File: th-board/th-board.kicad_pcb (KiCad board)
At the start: 2 copper layers, 59.5 x 48.5 mm, 21 parts, among them J1 Conn_01x02, J2 Conn_01x04, U1 ESP-12F, U2 DHT11, U3 SPX3819M5-L

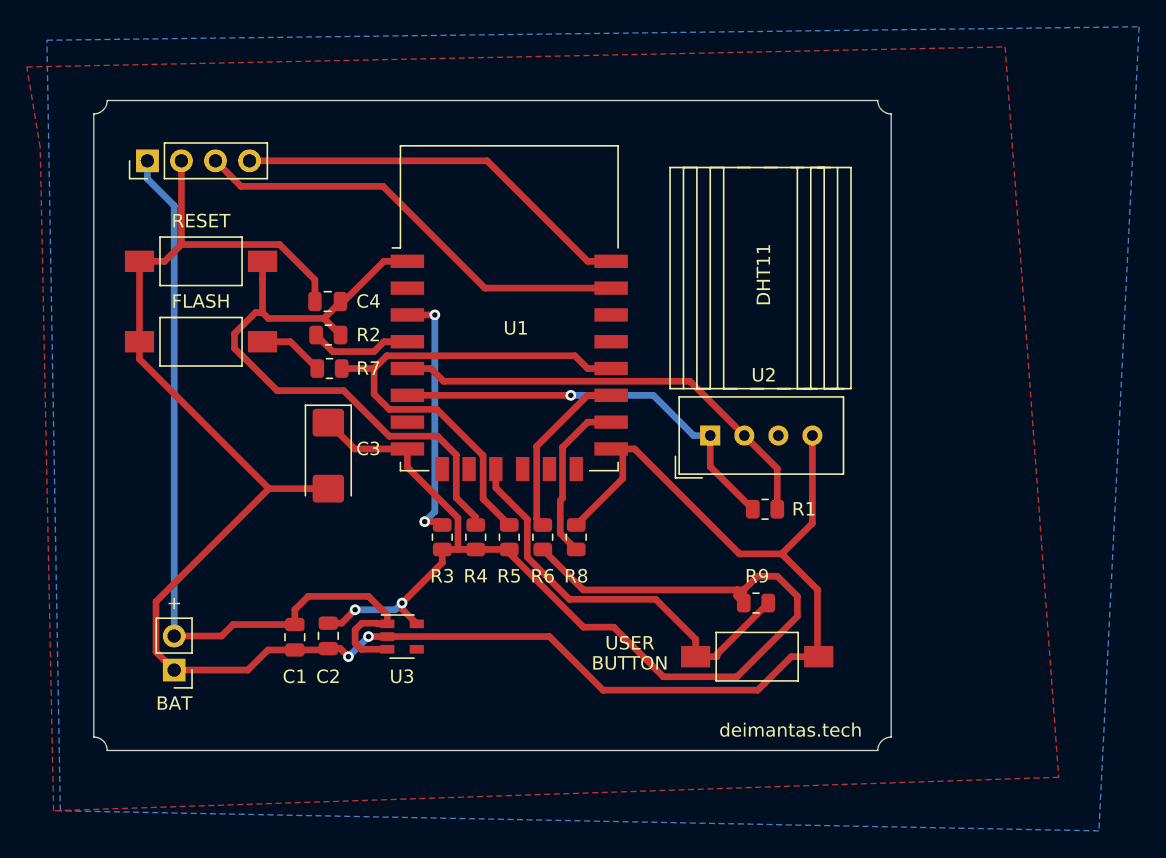
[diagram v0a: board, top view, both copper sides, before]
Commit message: Led added to pcb, v1.1
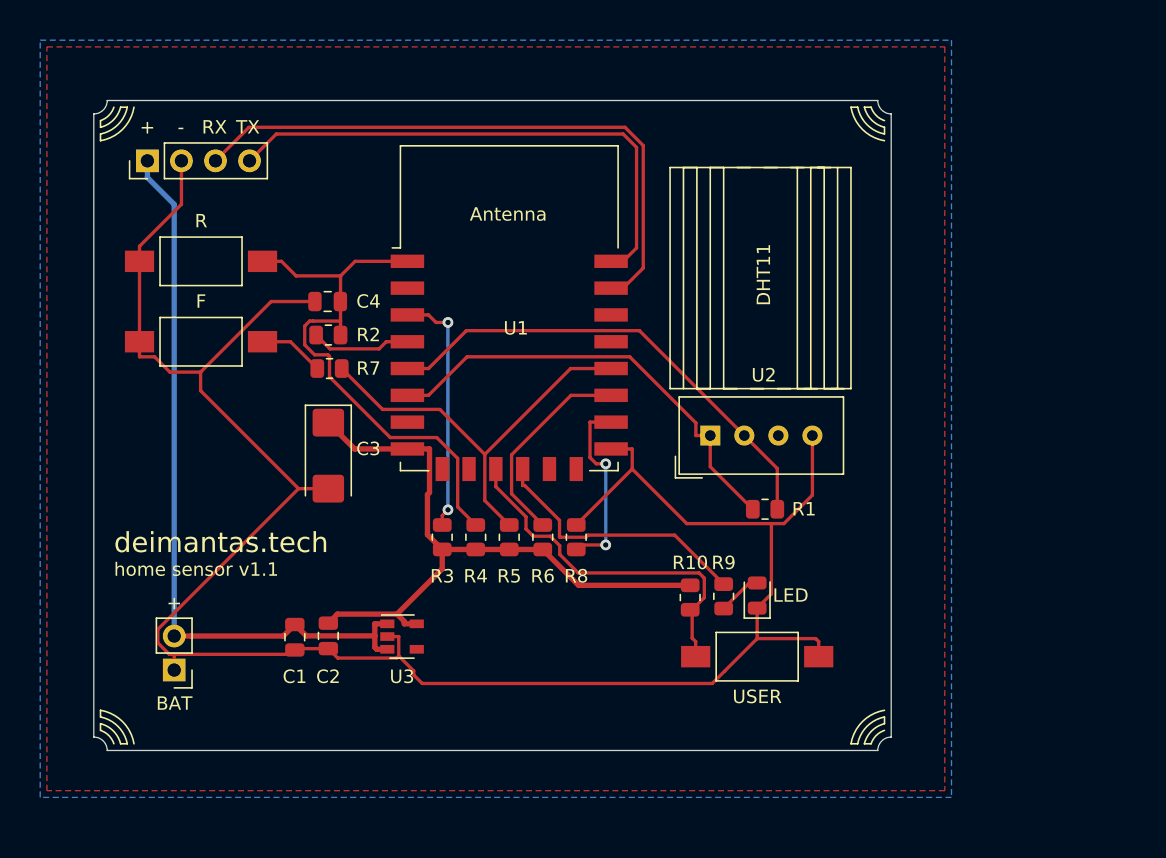
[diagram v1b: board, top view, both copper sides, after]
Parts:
- added D1: LED, LED_SMD:LED_0805_2012Metric, F.Cu at (168.5, 111.9)
- added R10: R470, Resistor_SMD:R_0805_2012Metric, F.Cu at (166.0, 112.0)
- moved R9 4.93 mm to (163.5, 112.1), turned to 90 degrees
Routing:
- net VCC: track 87.3 -> 49.5 mm, vias 2 -> 0
- net Net-(R10-Pad2): track 0.00 -> 20.1 mm
- net RX: track 33.5 -> 45.7 mm
- net TX: track 30.1 -> 39.9 mm
- net Net-(R5-Pad2): track 38.8 -> 31.4 mm
- net RST: track 48.0 -> 41.7 mm
- net Net-(C1-Pad1): track 61.5 -> 55.6 mm
- net Net-(R9-Pad1): track 31.1 -> 27.1 mm
- net Net-(D1-Pad2): track 0.00 -> 3.29 mm
- net DHT11_VCC: track 30.7 -> 33.6 mm, vias 1 -> 0
- net DHT11_IO: track 33.7 -> 36.1 mm
- net Net-(R6-Pad2): track 13.2 -> 15.5 mm
- net GND: track 159.5 -> 157.2 mm, vias 2 -> 0
- net Net-(R8-Pad1): track 12.6 -> 14.0 mm, vias 0 -> 2
- net Net-(R3-Pad2): track 19.2 -> 18.6 mm
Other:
- net class Default: trace_width 0.5 -> 0.25
- net class vcc added: clearance 0.2, trace_width 0.4, via_dia 0.8, via_drill 0.4
- board text added: "-"
- board text added: "F"
- board text added: "R"
- board text added: "RX"
- board text added: "TX"
- board text added: "home sensor v1.1"
- board text removed: "BUTTON"
- board text removed: "FLASH"
- board text removed: "RESET"

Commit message: PCB: new board
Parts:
- moved U2 76.5 mm to (241.5, 97.5)
- moved U1 75.8 mm to (225.8, 88.2)
- moved C1 75.0 mm to (209.0, 112.8)
- moved C2 75.0 mm to (211.5, 112.7)
- moved C3 75.0 mm to (211.5, 99.2)
- moved C4 75.0 mm to (211.4, 87.8)
- moved D1 75.0 mm to (243.5, 109.7)
- moved R1 75.0 mm to (244.1, 103.2)
- moved R10 75.0 mm to (241.0, 109.8)
- moved R2 75.0 mm to (211.5, 90.2)
- moved R3 75.0 mm to (220.0, 105.3)
- moved R4 75.0 mm to (222.5, 105.3)
- moved R5 75.0 mm to (225.0, 105.3)
- moved R6 75.0 mm to (227.5, 105.3)
- moved R7 75.0 mm to (211.6, 92.8)
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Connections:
- R10 pad 2: Net-(R10-Pad2) -> USER_LED
- R9 pad 1: Net-(R9-Pad1) -> USER_BUTTON
- SW_User2 pad 2: Net-(R9-Pad1) -> USER_BUTTON
- U1 pad 11: Net-(R9-Pad1) -> Net-(U1-Pad11)
- U1 pad 12: Net-(R10-Pad2) -> Net-(U1-Pad12)
- U1 pad 19: Net-(U1-Pad19) -> USER_BUTTON
- U1 pad 20: Net-(U1-Pad20) -> USER_LED
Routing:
- net GND: track 157.2 -> 194.4 mm, vias 0 -> 1
- net USER_BUTTON: track 0.00 -> 36.0 mm
- net USER_LED: track 0.00 -> 32.8 mm
- net Net-(R9-Pad1): track 27.1 -> 0.00 mm
- net Net-(R10-Pad2): track 20.1 -> 0.00 mm
- net Net-(C1-Pad1): track 55.6 -> 73.7 mm
- net RX: track 45.7 -> 35.8 mm
- net VCC: track 49.5 -> 57.5 mm
- net TX: track 39.9 -> 32.1 mm
- net Net-(R3-Pad2): track 18.6 -> 24.7 mm
- net Net-(R5-Pad2): track 31.4 -> 37.3 mm
- net Net-(R6-Pad2): track 15.5 -> 13.0 mm
- net DHT11_VCC: track 33.6 -> 31.6 mm
- net Net-(R7-Pad2): track 4.91 -> 6.87 mm
- net DHT11_IO: track 36.1 -> 34.7 mm
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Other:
- board size 59.5 x 48.5 mm -> 65 x 55 mm
- board text added: "DEIMANTAS.TECH"
- board text added: "Flash"
- board text added: "Reset"
- board text removed: "F"
- board text removed: "R"
- board text removed: "deimantas.tech"

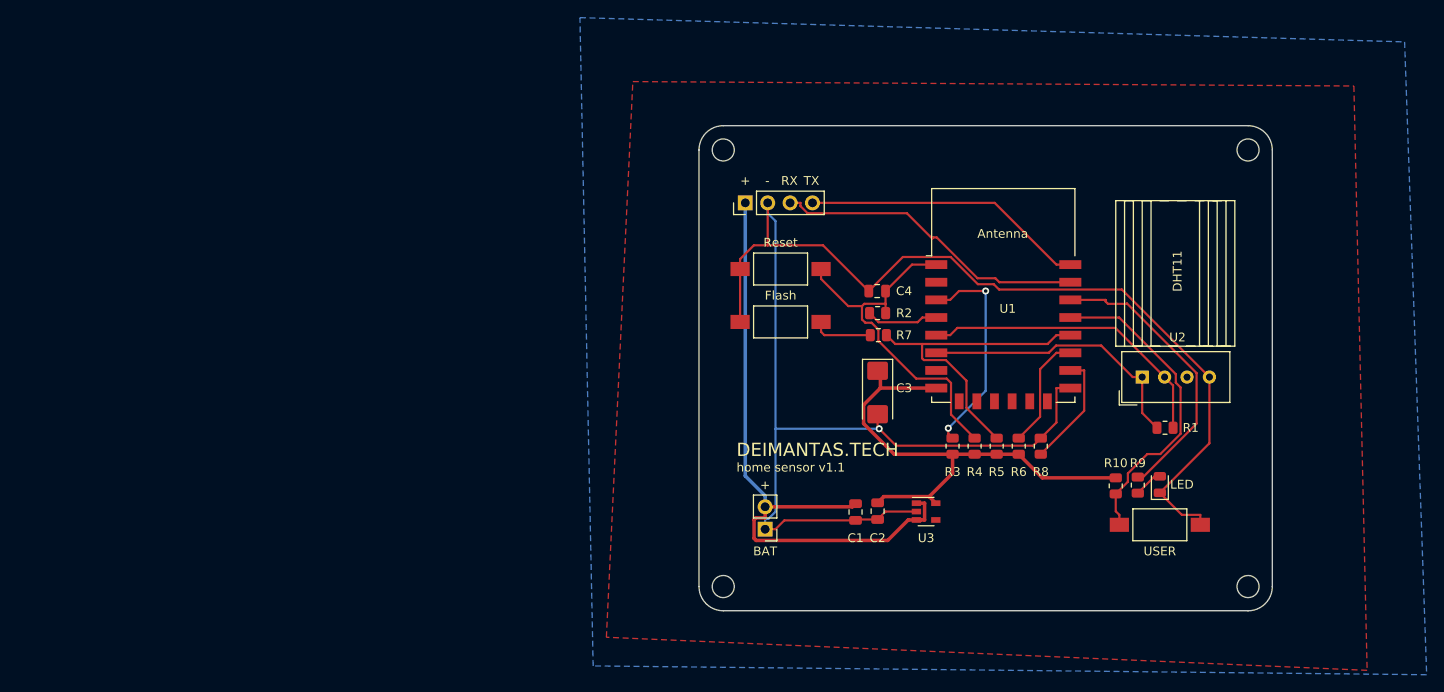
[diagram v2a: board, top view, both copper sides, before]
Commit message: PCB: smaller board
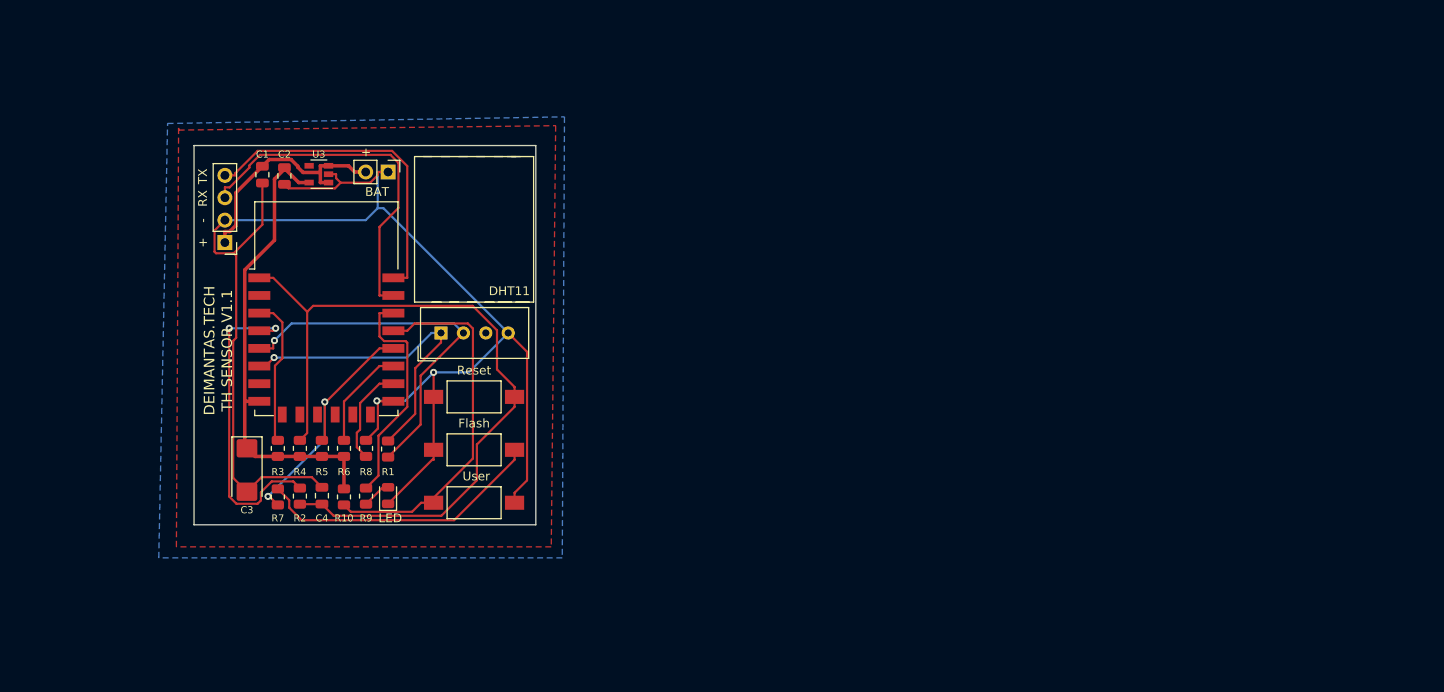
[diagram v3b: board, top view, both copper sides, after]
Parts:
- moved R1 88.1 mm to (156.0, 105.7), turned to 270 degrees
- moved D1 87.5 mm to (156.0, 110.9)
- moved R10 87.5 mm to (153.5, 111.0)
- moved R9 87.5 mm to (151.0, 111.1)
- moved U2 79.7 mm to (162.0, 92.5)
- moved U3 78.8 mm to (148.2, 74.5), turned to 180 degrees
- moved SW_User2 77.8 mm to (165.8, 111.8)
- moved C1 77.4 mm to (141.8, 74.5)
- moved C2 77.2 mm to (144.2, 74.7)
- moved U1 76.8 mm to (149.0, 89.8)
- moved R3 76.5 mm to (143.5, 105.6)
- moved R4 76.5 mm to (146.0, 105.6)
- moved R5 76.5 mm to (148.5, 105.6)
- moved R6 76.5 mm to (151.0, 105.6)
- moved R8 76.5 mm to (153.5, 105.6)
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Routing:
- net Net-(C1-Pad1): track 73.7 -> 26.6 mm
- net RST: track 42.0 -> 86.8 mm
- net Net-(R2-Pad2): track 8.21 -> 36.6 mm, vias 0 -> 2
- net Net-(R7-Pad2): track 6.87 -> 32.8 mm
- net GND: track 194.4 -> 174.8 mm, vias 1 -> 2
- net DHT11_IO: track 34.7 -> 42.8 mm, vias 0 -> 1
- net Net-(R3-Pad2): track 24.7 -> 16.9 mm, vias 2 -> 0
- net Net-(R5-Pad2): track 37.3 -> 29.7 mm, vias 0 -> 2
- net USER_LED: track 32.8 -> 26.1 mm
- net USER_BUTTON: track 36.0 -> 42.1 mm
- net DHT11_VCC: track 31.6 -> 36.9 mm, vias 0 -> 1
- net TX: track 32.1 -> 36.9 mm
- net RX: track 35.8 -> 40.4 mm
- net VCC: track 57.5 -> 53.9 mm
- net Net-(R8-Pad1): track 13.1 -> 11.3 mm
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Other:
- board size 65 x 55 mm -> 38.8 x 43 mm
- board text added: "TH SENSOR V1.1"
- board text added: "User"
- board text removed: "USER"
- board text removed: "home sensor v1.1"

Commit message: PCB: very small pcb :)
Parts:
- removed SW_Flash1: SW_Push, Button_Switch_SMD:SW_SPST_FSMSM
- added J3: Conn_01x02, Connector_PinHeader_2.54mm:PinHeader_1x02_P2.54mm_Vertical, F.Cu at (150.5, 110.5)
- moved J2 23.3 mm to (155.8, 67.8), turned to 90 degrees
- moved R1 20.1 mm to (150.7, 86.2), turned to 0 degrees
- moved C3 18.5 mm to (156.5, 99.8)
- moved R8 17.1 mm to (150.6, 88.8), turned to 180 degrees
- moved U1 16.0 mm to (163.0, 82.0)
- moved J1 15.5 mm to (170.0, 67.8)
- moved U2 15.1 mm to (169.2, 105.8), turned to 180 degrees
- moved R6 14.3 mm to (150.6, 91.2), turned to 180 degrees
- moved R5 12.0 mm to (150.6, 93.8), turned to 180 degrees
- moved C1 11.2 mm to (150.7, 81.2), turned to 180 degrees
- moved C2 11.0 mm to (150.6, 83.8), turned to 180 degrees
- moved R2 11.0 mm to (150.5, 101.0), turned to 180 degrees
- moved R4 10.4 mm to (150.6, 96.2), turned to 180 degrees
- moved R7 10.4 mm to (150.6, 103.5), turned to 180 degrees
- moved R3 9.85 mm to (150.6, 98.8), turned to 180 degrees
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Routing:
- net GND: track 174.8 -> 138.4 mm, vias 2 -> 1
- net Net-(J3-Pad2): track 32.8 -> 4.80 mm
- net RX: track 40.4 -> 17.7 mm
- net TX: track 36.9 -> 14.7 mm
- net Net-(R8-Pad1): track 11.3 -> 33.1 mm, vias 0 -> 2
- net Net-(C1-Pad1): track 26.6 -> 44.1 mm, vias 0 -> 1
- net Net-(R6-Pad2): track 11.7 -> 26.6 mm, vias 0 -> 2
- net DHT11_VCC: track 36.9 -> 50.3 mm, vias 1 -> 2
- net USER_BUTTON: track 42.1 -> 53.8 mm
- net RST: track 86.8 -> 76.7 mm
- net Net-(R5-Pad2): track 29.7 -> 39.5 mm, vias 2 -> 3
- net USER_LED: track 26.1 -> 35.9 mm, vias 0 -> 2
- net Net-(R3-Pad2): track 16.9 -> 23.4 mm, vias 0 -> 2
- net Net-(R2-Pad2): track 36.6 -> 30.4 mm
- net DHT11_IO: track 42.8 -> 36.9 mm
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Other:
- board size 38.8 x 43 mm -> 24.2 x 48.5 mm
- board text added: "DEIMANTAS.TECH TH SENSOR V1.1"
- board text removed: "+"
- board text removed: "-"
- board text removed: "BAT"
- board text removed: "DEIMANTAS.TECH"
- board text removed: "Flash"
- board text removed: "RX"
- board text removed: "TH SENSOR V1.1"
- board text removed: "TX"

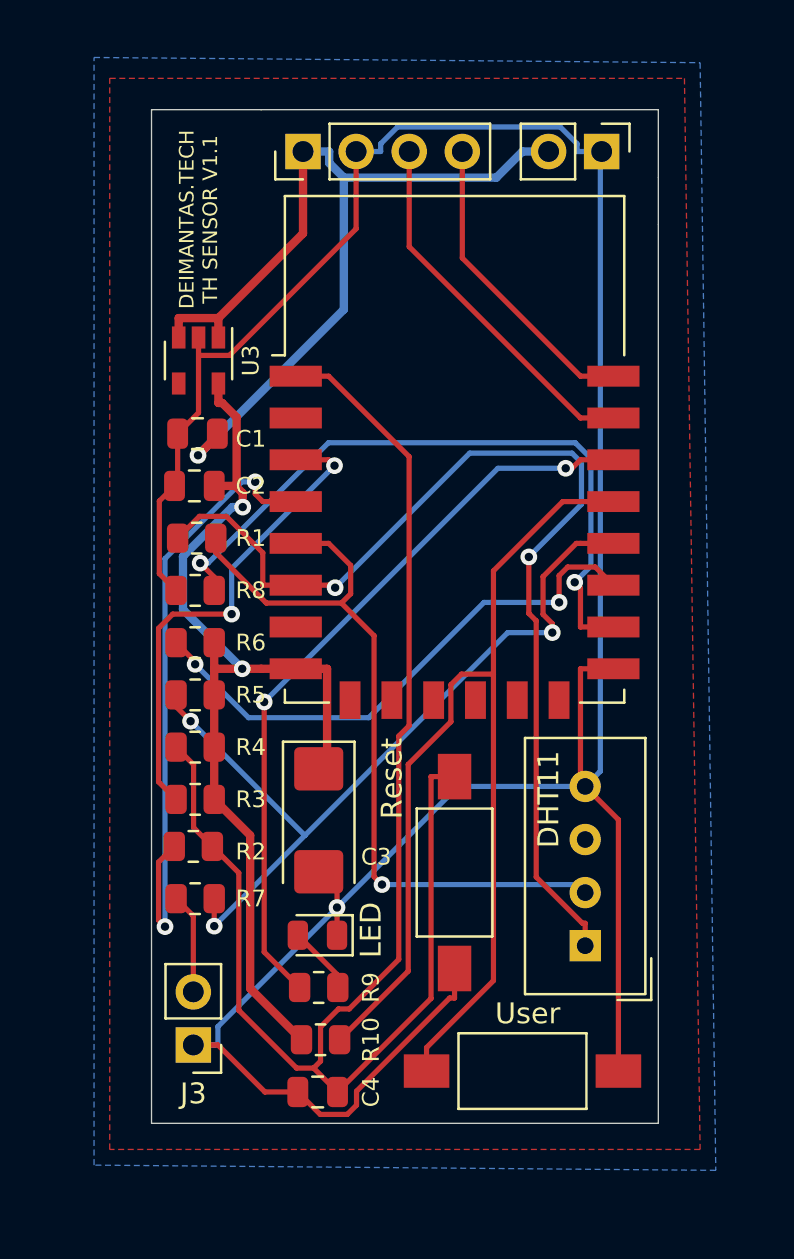
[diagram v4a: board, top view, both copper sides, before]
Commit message: PCB: some rearranges
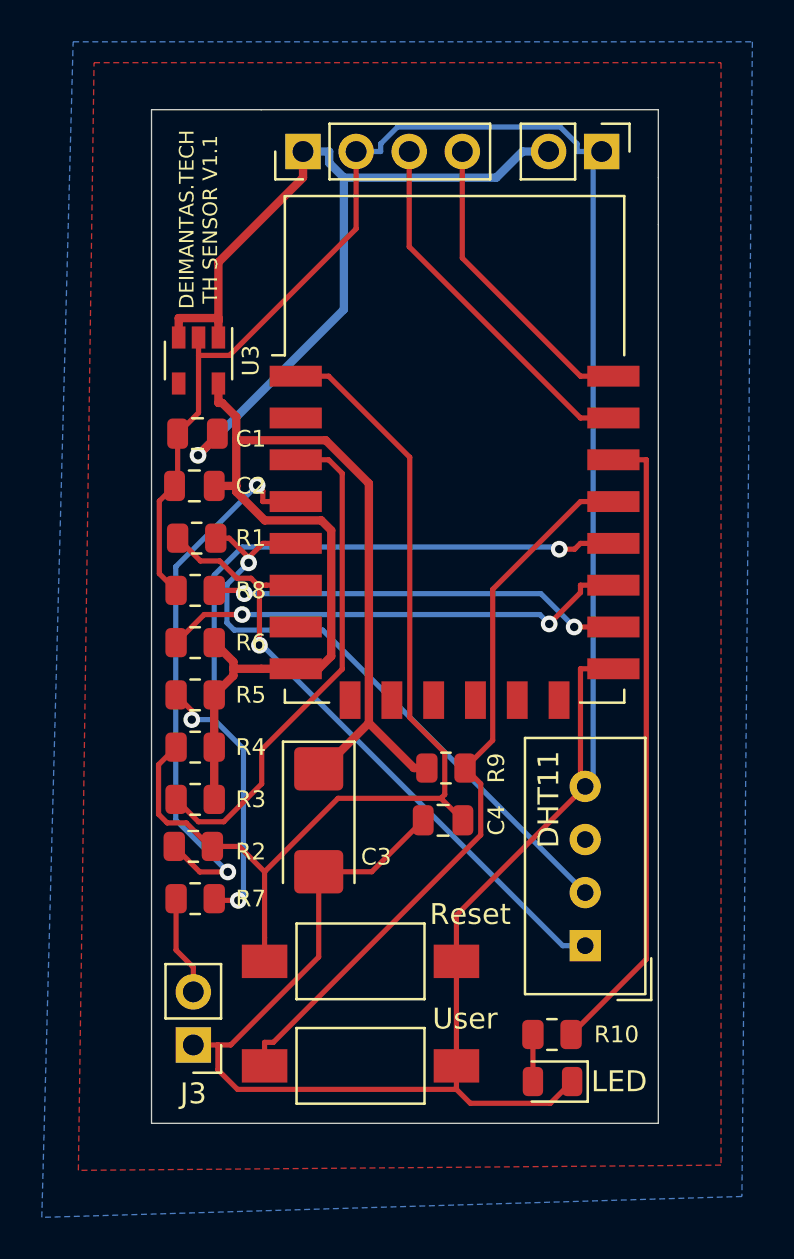
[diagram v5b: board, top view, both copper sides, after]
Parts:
- moved C4 14.3 mm to (162.4, 99.8)
- moved R9 14.3 mm to (162.6, 97.2)
- moved D1 13.2 mm to (167.7, 112.2)
- moved R10 11.4 mm to (167.7, 110.0), turned to 0 degrees
- moved SW_User2 7.75 mm to (158.5, 111.5)
- moved SW_User1 6.19 mm to (158.5, 106.5), turned to 0 degrees
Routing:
- net RST: track 76.7 -> 49.6 mm
- net DHT11_VCC: track 50.3 -> 31.0 mm, vias 2 -> 1
- net USER_BUTTON: track 53.8 -> 35.7 mm
- net Net-(R8-Pad1): track 33.1 -> 19.8 mm
- net VCC: track 49.0 -> 56.9 mm, vias 2 -> 0
- net DHT11_IO: track 36.9 -> 30.5 mm
- net GND: track 138.4 -> 132.1 mm, vias 1 -> 0
- net USER_LED: track 35.9 -> 30.6 mm, vias 2 -> 0
- net Net-(R6-Pad2): track 26.6 -> 22.6 mm
- net Net-(R2-Pad2): track 30.4 -> 26.7 mm
- net Net-(D1-Pad2): track 3.29 -> 2.25 mm
- net Net-(R3-Pad2): track 23.4 -> 24.2 mm, vias 2 -> 0
